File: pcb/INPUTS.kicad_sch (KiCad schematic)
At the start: 0 parts

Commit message: updated ethernet
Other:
- sheet INPUT_20V_0 ports: added 3V3; removed none
- sheet INPUT_20V_1 ports: added 3V3; removed none
- sheet INPUT_20V_12V ports: added 3V3; removed none
- sheet INPUT_20V_2 ports: added 3V3; removed none
- sheet INPUT_20V_3 ports: added 3V3; removed none
- sheet INPUT_5V_0 ports: added 3V3; removed none
- sheet INPUT_5V_1 ports: added 3V3; removed none
- sheet INPUT_5V_2 ports: added 3V3; removed none
- sheet INPUT_5V_3 ports: added 3V3; removed none

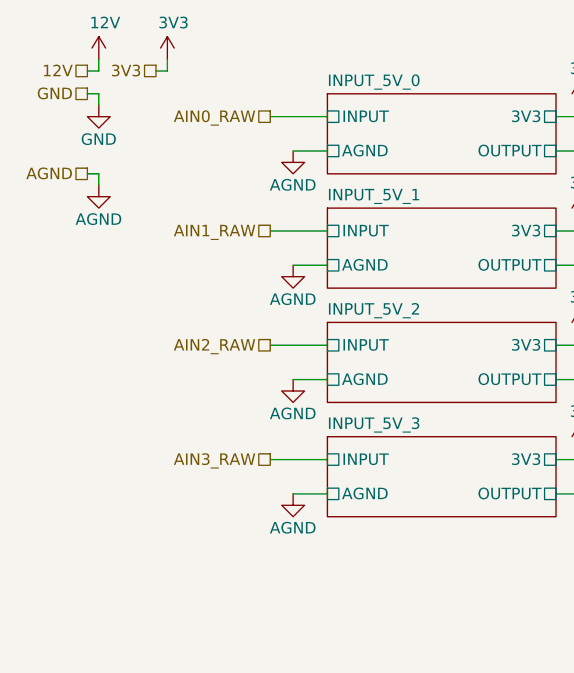
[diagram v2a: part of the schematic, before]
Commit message: removed AGND and added ground garden
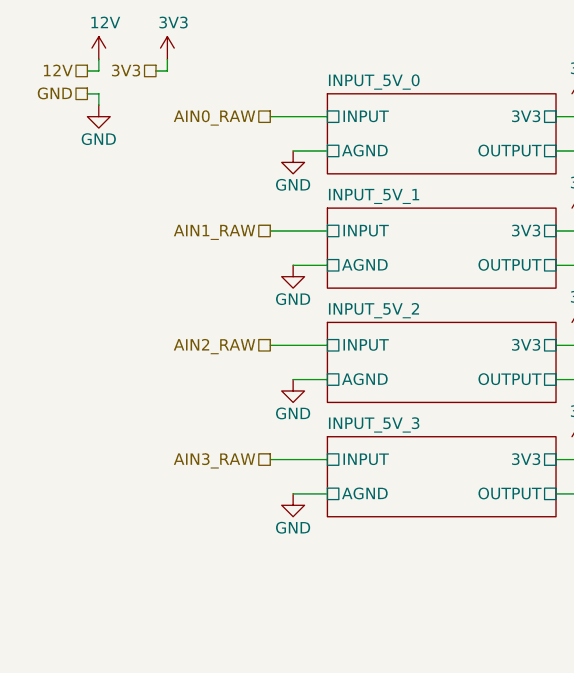
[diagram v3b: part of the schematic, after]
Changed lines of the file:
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@@
-	(wire
-		(pts
-			(xy 25.4 34.29) (xy 25.4 35.56)
-		)
-		(stroke
-			(width 0)
-			(type default)
-		)
-	)
 	(wire
 		(pts
@@
 	(wire
 		(pts
-			(xy 25.4 34.29) (xy 24.13 34.29)
-		)
-		(stroke
-			(width 0)
-			(type default)
-		)
-	)
-	(wire
-		(pts
 			(xy 78.74 53.34) (xy 76.2 53.34)
 		)
@@
 		(shape passive)
 		(at 24.13 25.4 180)
-		(effects
-			(font
-				(size 1.27 1.27)
-			)
-			(justify right)
-		)
-	)
-	(hierarchical_label "AGND"
-		(shape passive)
-		(at 24.13 34.29 180)
 		(effects
 			(font
@@
 			)
 		)
-		(property "Value" "AGND"
+		(property "Value" "GND"
 			(at 46.99 73.66 0)
 			(effects
@@
 	)
 	(symbol
-		(lib_id "power:GND")
-		(at 25.4 35.56 0)
-		(unit 1)
-		(exclude_from_sim no)
-		(in_bom yes)
-		(on_board yes)
-		(dnp no)
-		(property "Reference" "#PWR0142"
-			(at 25.4 41.91 0)
-			(effects
-				(font
-					(size 1.27 1.27)
-				)
-				(hide yes)
-			)
-		)
-		(property "Value" "AGND"
-			(at 25.4 39.37 0)
-			(effects
-				(font
-					(size 1.27 1.27)
-				)
-			)
-		)
-		(property "Footprint" ""
-			(at 25.4 35.56 0)
-			(effects
-				(font
-					(size 1.27 1.27)
-				)
-				(hide yes)
-			)
-		)
-		(property "Datasheet" ""
-			(at 25.4 35.56 0)
-			(effects
-				(font
-					(size 1.27 1.27)
-				)
-				(hide yes)
-			)
-		)
-		(property "Description" "Power symbol creates a global label with name \"GND\" , ground"
-			(at 25.4 35.56 0)
-			(effects
-				(font
-					(size 1.27 1.27)
-				)
-				(hide yes)
-			)
-		)
-		(pin "1"
-		)
-		(instances
-			(project "NCU"
-				(path "/3aee14c3-5480-4f7c-989e-3fef81779034/85ee8b65-a216-46f6-943b-de278ee684a4"
-					(reference "#PWR0142")
-					(unit 1)
-				)
-			)
-		)
-	)
-	(symbol
 		(lib_id "power:+3V3")
 		(at 154.94 52.07 0)
@@
 			)
 		)
-		(property "Value" "AGND"
+		(property "Value" "GND"
 			(at 46.99 60.96 0)
 			(effects
@@
 			)
 		)
-		(property "Value" "AGND"
+		(property "Value" "GND"
 			(at 46.99 48.26 0)
 			(effects
@@
 			)
 		)
-		(property "Value" "AGND"
+		(property "Value" "GND"
 			(at 46.99 35.56 0)
 			(effects

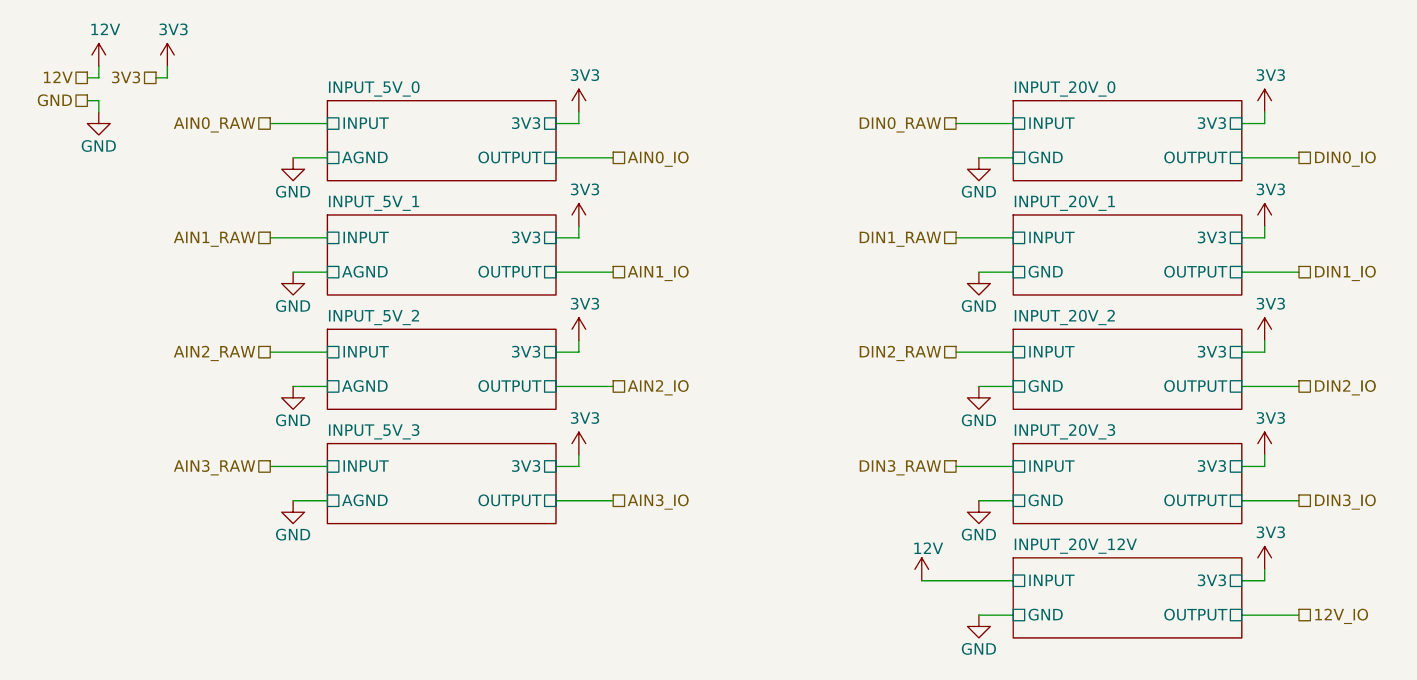
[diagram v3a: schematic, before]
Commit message: added 10k resistor to USB VBUS line
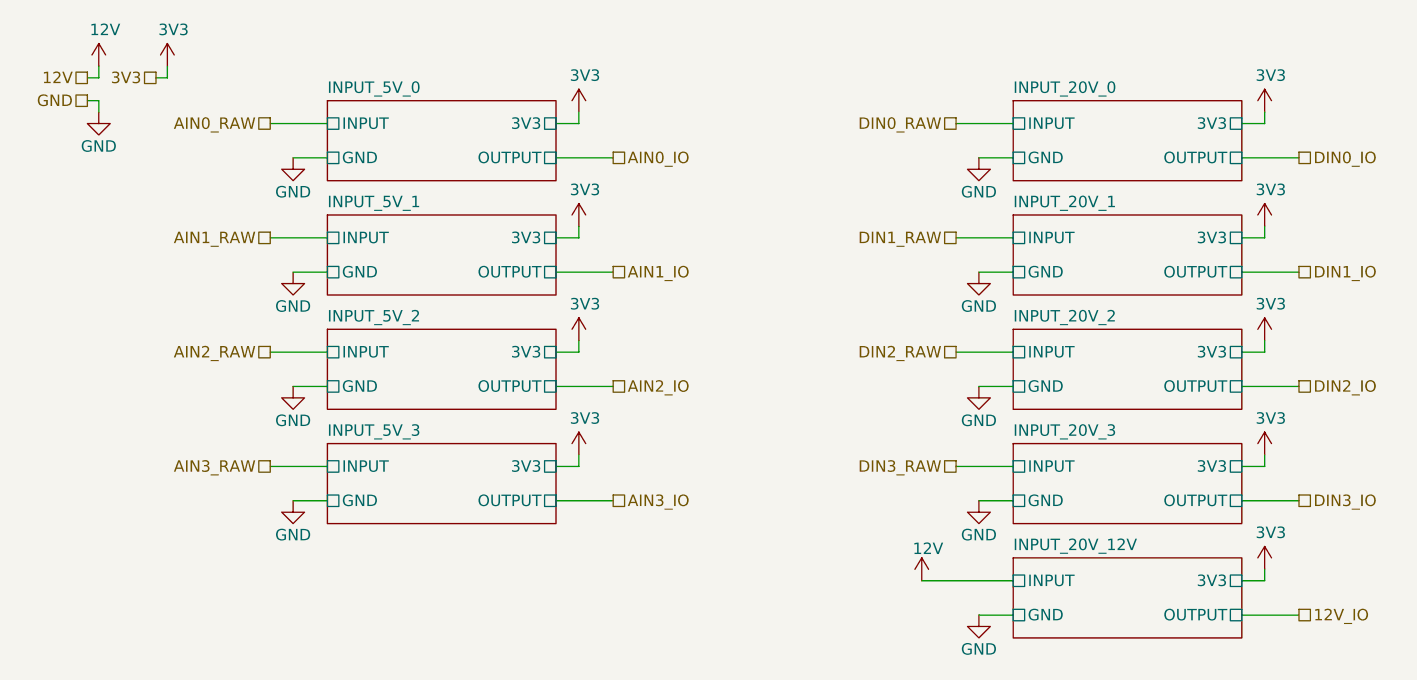
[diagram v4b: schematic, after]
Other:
- sheet INPUT_5V_0 ports: added GND; removed AGND
- sheet INPUT_5V_1 ports: added GND; removed AGND
- sheet INPUT_5V_2 ports: added GND; removed AGND
- sheet INPUT_5V_3 ports: added GND; removed AGND
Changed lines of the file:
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@@
 			)
 		)
-		(pin "AGND" passive
+		(pin "GND" passive
 			(at 50.8 69.85 180)
 			(effects
@@
 			)
 		)
-		(pin "AGND" passive
+		(pin "GND" passive
 			(at 50.8 57.15 180)
 			(effects
@@
 			)
 		)
-		(pin "AGND" passive
+		(pin "GND" passive
 			(at 50.8 31.75 180)
 			(effects
@@
 			)
 		)
-		(pin "AGND" passive
+		(pin "GND" passive
 			(at 50.8 44.45 180)
 			(effects
